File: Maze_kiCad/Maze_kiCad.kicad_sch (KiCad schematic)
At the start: 23 parts, among them J1 Screw_Terminal, J10 pins: 42_41_40_39_38_37, J11 pins: 36_35_0_45_34_33_21, J2 motor2, J3 motor1, J4 Vmm/Mode, J5 gyro_pins, J6 GNd, J7 IR Receiver, J8 pins: 5v/12_11_10_9_46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

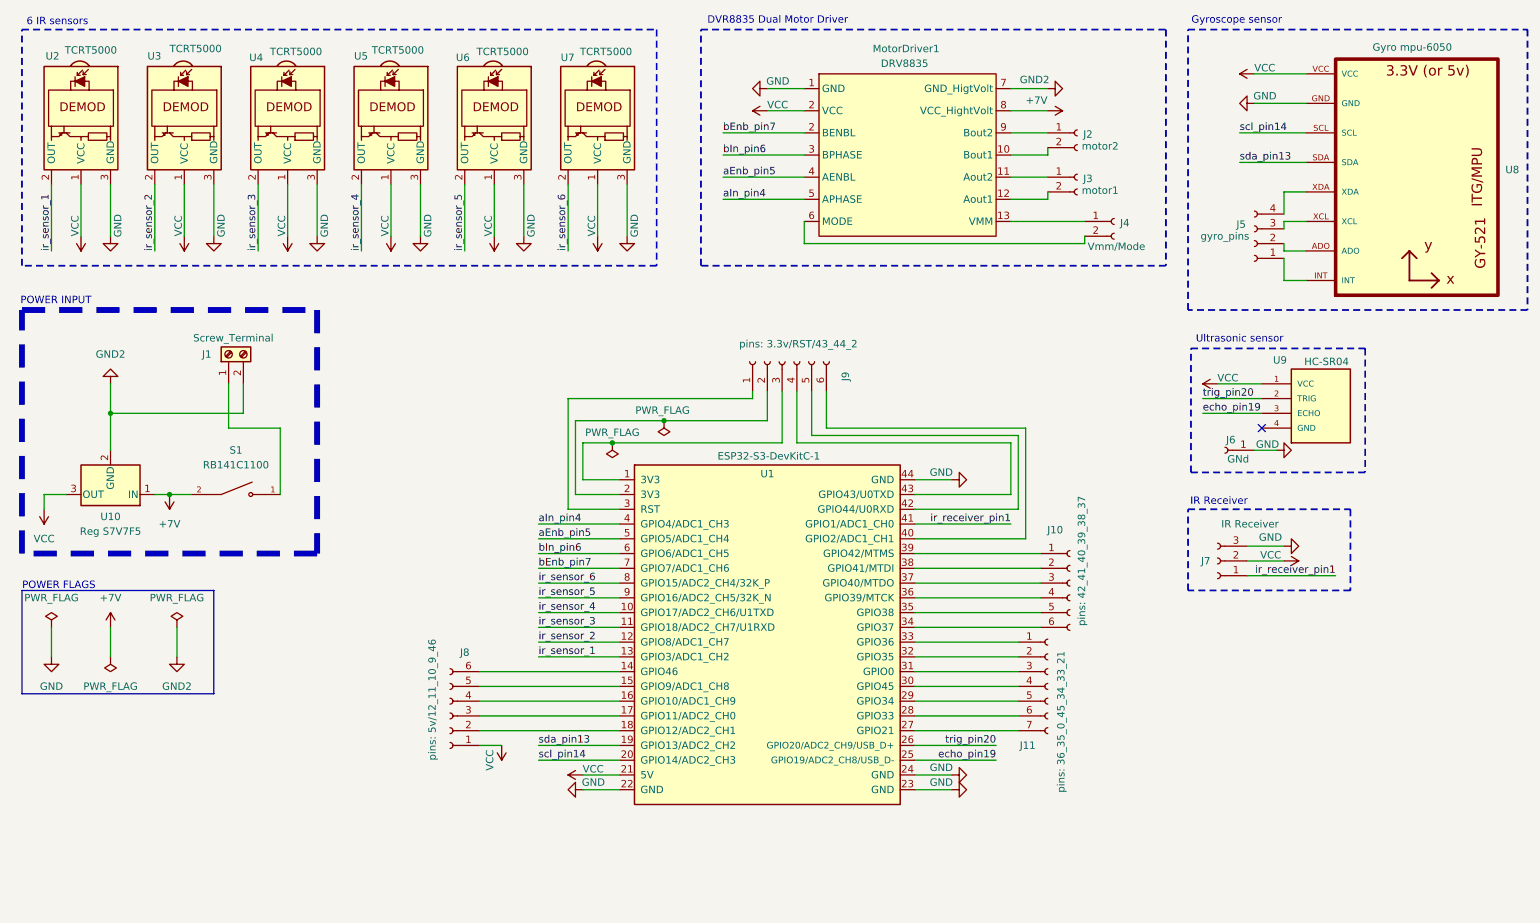
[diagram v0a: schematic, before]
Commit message: Add two RGB LEDs to the circuit schematic
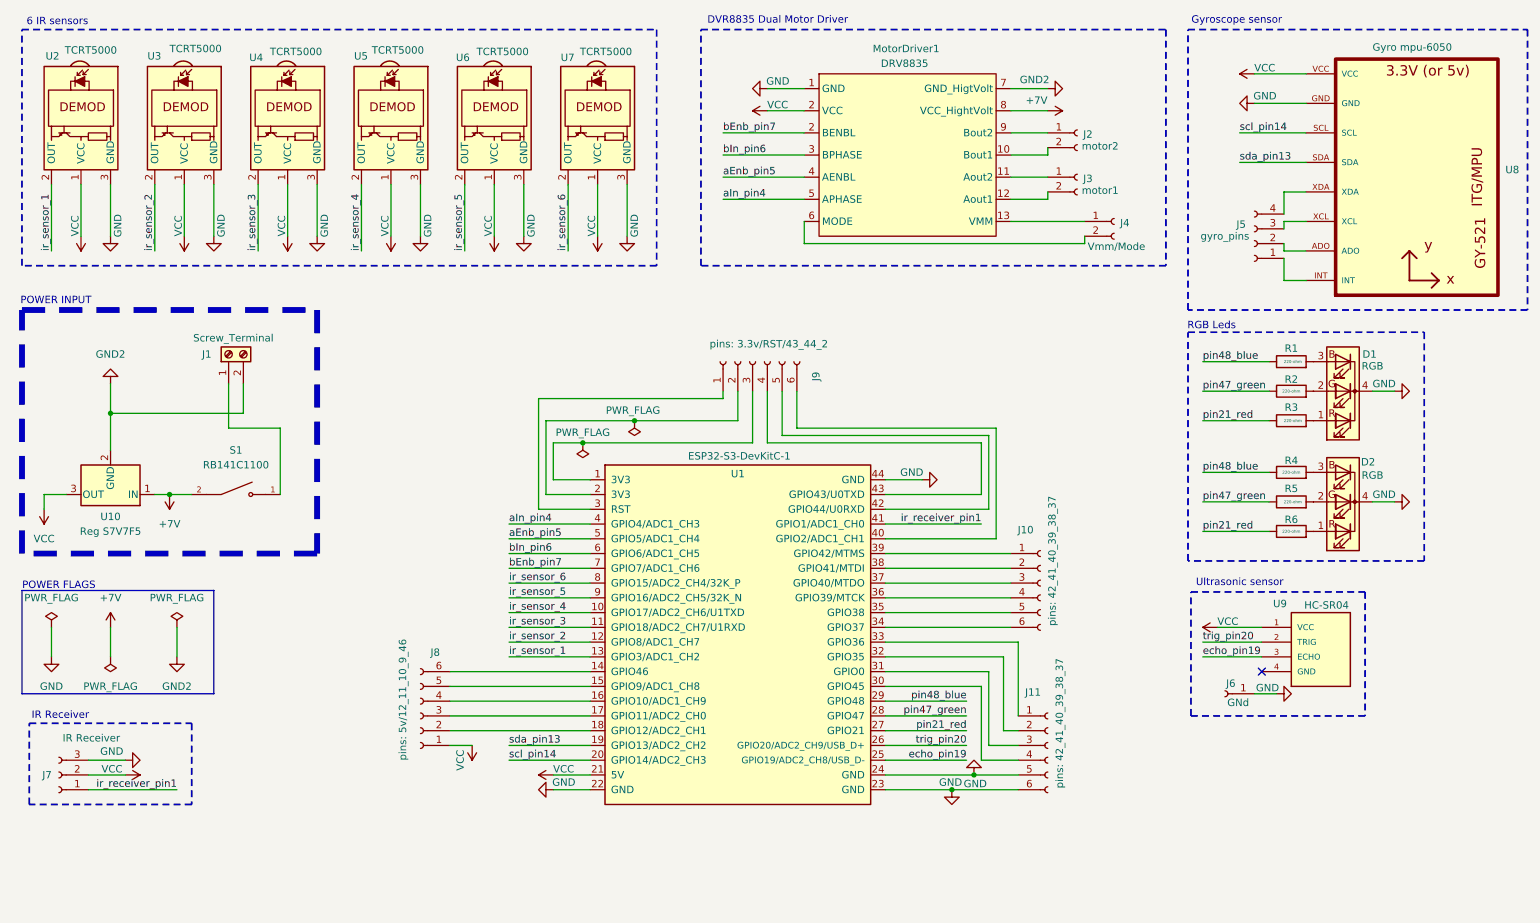
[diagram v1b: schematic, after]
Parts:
- removed J11: pins: 36_35_0_45_34_33_21, symbol Connector:Conn_01x07_Socket
- added D1, D2: RGB, LED_SMD:LED_LiteOn_LTST-E563C_PLCC4_5.0x5.0mm_P3.2mm_HandSoldering, symbol Device:LED_RGBK
- added J11: pins: 42_41_40_39_38_37, symbol Connector:Conn_01x06_Socket
- added R1, R2, R3, R4, R5, R6: 220-ohm, symbol Device:R
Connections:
- net GND: now also D1.4 (K), D2.4 (K), J11.5 (Pin_5), J11.6 (Pin_6)
- net at U1.33 (GPIO36): now also J11.1 (Pin_1)
- net at U1.32 (GPIO35): now also J11.2 (Pin_2)
- net at U1.31 (GPIO0): now also J11.3 (Pin_3)
- net at U1.30 (GPIO45): now also J11.4 (Pin_4)
- net pin48_blue: now reaches U1.29 (GPIO48)
- net pin48_blue: now also R1.1, R4.1
- net pin47_green: now reaches U1.28 (GPIO47)
- net pin47_green: now also R2.1, R5.1
- net pin21_red: now reaches U1.27 (GPIO21)
- net pin21_red: now also R3.1, R6.1
- new net: D1.1 (RA), R3.2
- new net: D1.2 (GA), R2.2
- new net: D2.3 (BA), R4.2
- new net: D2.2 (GA), R5.2
- new net: D2.1 (RA), R6.2
- new net: D1.3 (BA), R1.2
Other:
- note added: "RGB Leds"
- moved on the sheet: J10, J6, J7, J8, J9, U1, U9

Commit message: assign footprints
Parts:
- added J12: Vcc/Gnd, Connector_PinSocket_2.54mm:PinSocket_1x04_P2.54mm_Vertical, symbol Connector:Conn_01x04_Socket
- D1, D2: footprint LED_SMD:LED_LiteOn_LTST-E563C_PLCC4_5.0x5.0mm_P3.2mm_HandSoldering -> LED_THT:LED_D5.0mm-4_RGB_Staggered_Pins
- J10, J11, J8, J9: footprint (none) -> Connector_PinSocket_2.54mm:PinSocket_1x06_P2.54mm_Vertical
- J5: value gyro_pins -> INT/ADO/XCL/XDA; footprint (none) -> Connector_PinSocket_2.54mm:PinSocket_1x04_P2.54mm_Vertical
- J6: value GNd -> GND; footprint (none) -> Connector_PinSocket_2.54mm:PinSocket_1x01_P2.54mm_Vertical
- J7: footprint (none) -> Connector_PinSocket_2.54mm:PinSocket_1x03_P2.54mm_Vertical
- R1, R2, R3, R4, R5, R6: footprint (none) -> Resistor_THT:R_Axial_DIN0204_L3.6mm_D1.6mm_P7.62mm_Horizontal
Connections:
- net +7V: now also MotorDriver1.9 (VCC_HightVolt); no longer MotorDriver1.8 (VCC_HightVolt)
- net GND: now also J12.1 (Pin_1), J12.2 (Pin_2)
- net GND2: now also MotorDriver1.8 (GND_HigtVolt); no longer MotorDriver1.7 (GND_HigtVolt)
- net VCC: now also J12.3 (Pin_3), J12.4 (Pin_4)
- net aEnb_pin5: now also MotorDriver1.5 (AENBL); no longer MotorDriver1.4 (AENBL)
- net aIn_pin4: now also MotorDriver1.6 (APHASE); no longer MotorDriver1.5 (APHASE)
- net bEnb_pin7: now also MotorDriver1.3 (BENBL); no longer MotorDriver1.2 (VCC)
- net bIn_pin6: now also MotorDriver1.4 (BPHASE); no longer MotorDriver1.3 (BPHASE)
- net at J4.1 (Pin_1): now also MotorDriver1.14 (VMM); no longer MotorDriver1.13 (VMM)
- net at J4.2 (Pin_2): now also MotorDriver1.7 (MODE); no longer MotorDriver1.6 (MODE)
- net at J2.1 (Pin_1): now also MotorDriver1.10 (Bout2); no longer MotorDriver1.9 (Bout2)
- net at J2.2 (Pin_2): now also MotorDriver1.11 (Bout1); no longer MotorDriver1.10 (Bout1)
- net at J3.1 (Pin_1): now also MotorDriver1.12 (Aout2); no longer MotorDriver1.11 (Aout2)
- net at J3.2 (Pin_2): now also MotorDriver1.13 (Aout1); no longer MotorDriver1.12 (Aout1)

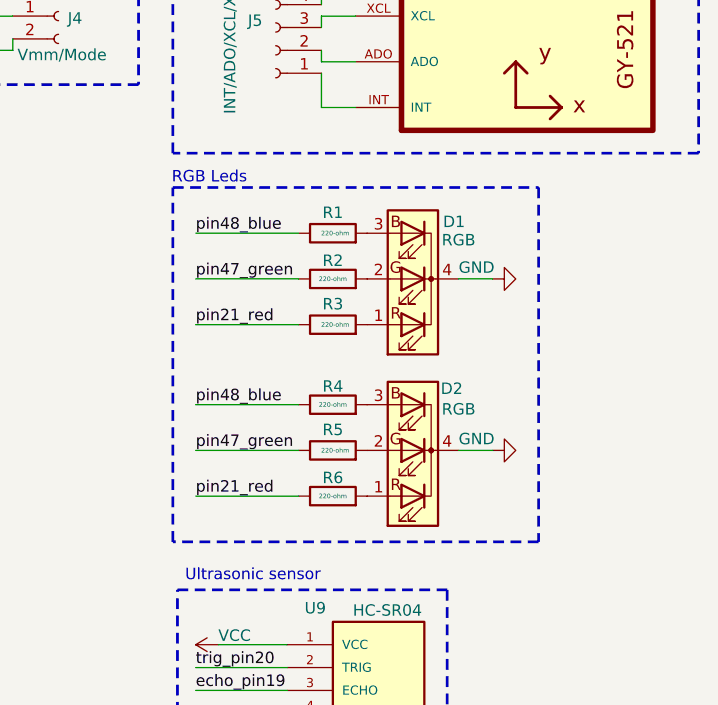
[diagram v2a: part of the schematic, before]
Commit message: Remove the resistors because the two LEDs use the same pins
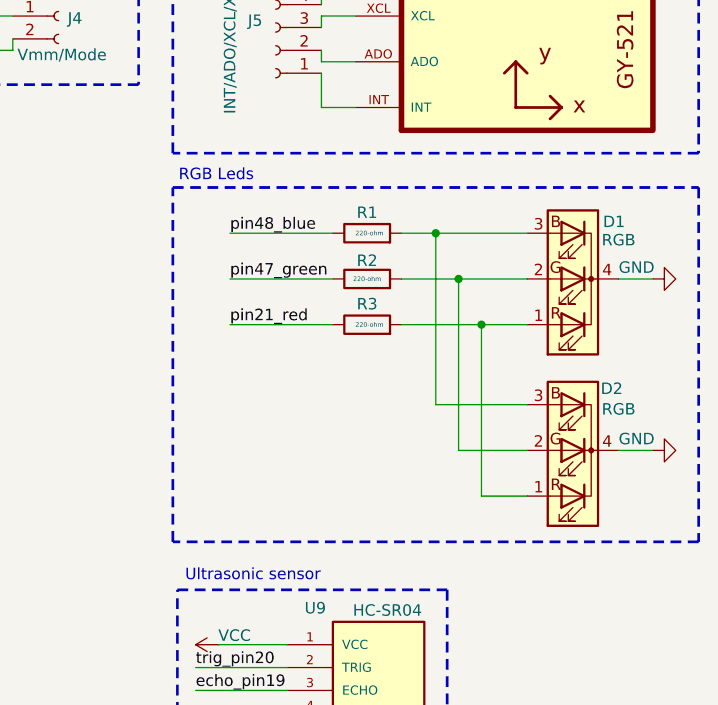
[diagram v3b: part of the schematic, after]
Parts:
- removed R4, R5, R6: 220-ohm, Resistor_THT:R_Axial_DIN0204_L3.6mm_D1.6mm_P7.62mm_Horizontal, symbol Device:R
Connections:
- net at D1.1 (RA), R3.2: now also D2.1 (RA)
- net at D1.2 (GA), R2.2: now also D2.2 (GA)
- net at D2.3 (BA): now also D1.3 (BA), R1.2
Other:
- moved on the sheet: D1, D2, R1, R2, R3

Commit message: Create version 1 of pcb
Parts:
- J1: footprint TerminalBlock_Phoenix:TerminalBlock_Phoenix_MPT-0,5-2-2.54_1x02_P2.54mm_Horizontal -> TerminalBlock_Phoenix:TerminalBlock_Phoenix_MKDS-1,5-2_1x02_P5.00mm_Horizontal
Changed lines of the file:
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@@
 			)
 		)
-		(property "Footprint" "TerminalBlock_Phoenix:TerminalBlock_Phoenix_MPT-0,5-2-2.54_1x02_P2.54mm_Horizontal"
+		(property "Footprint" "TerminalBlock_Phoenix:TerminalBlock_Phoenix_MKDS-1,5-2_1x02_P5.00mm_Horizontal"
 			(at 53.34 74.93 0)
 			(effects

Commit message: Final maze robot pcb
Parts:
- J11: value pins: 42_41_40_39_38_37 -> pins: gnd_gnd_45_0_35_36
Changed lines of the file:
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@@
 			)
 		)
-		(property "Value" "pins: 42_41_40_39_38_37"
+		(property "Value" "pins: gnd_gnd_45_0_35_36"
 			(at 196.342 138.43 90)
 			(effects
